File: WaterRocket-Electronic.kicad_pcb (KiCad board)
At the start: 2 copper layers, 60 x 60 mm, 9 parts, among them J1 Screw_Terminal_01x02, SW1 SW_SPDT, U1 MPU_6050

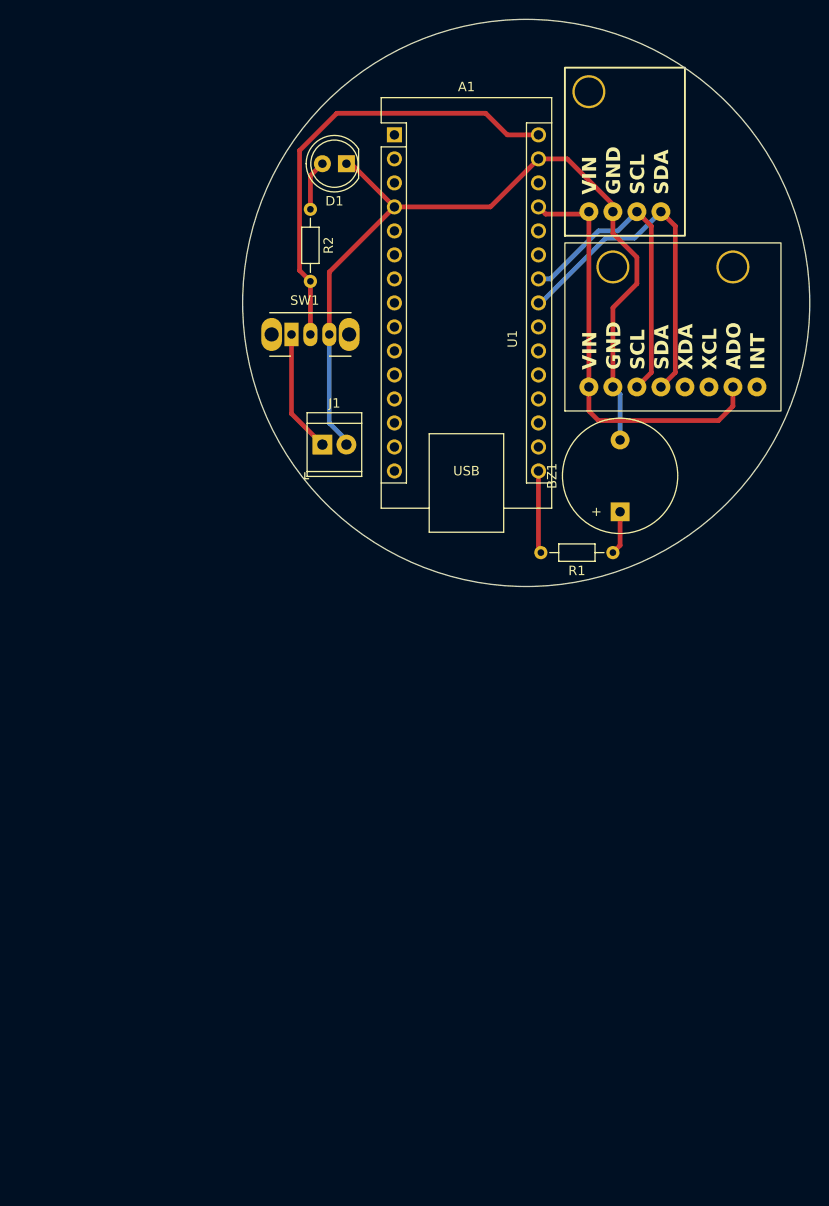
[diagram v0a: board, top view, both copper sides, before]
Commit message: Added servomotor, exported
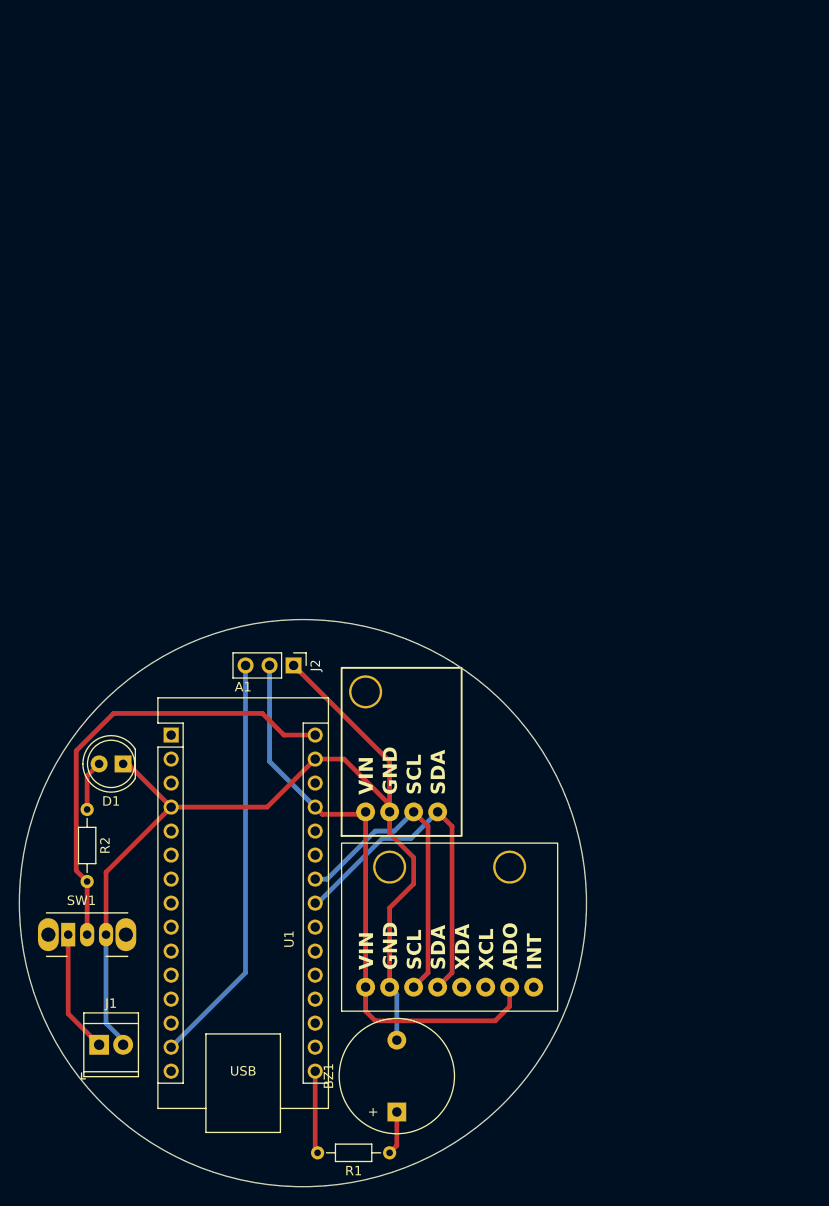
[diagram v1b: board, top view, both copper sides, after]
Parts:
- added J2: Conn_01x03, Connector_PinHeader_2.54mm:PinHeader_1x03_P2.54mm_Vertical, F.Cu at (102.9, 114.8)
- moved J1 67.8 mm to (82.3, 154.9)
- moved R2 67.8 mm to (81.0, 130.0)
- moved SW1 67.8 mm to (79.0, 143.3)
- moved U1 67.8 mm to (110.5, 148.8)
- moved A1 67.8 mm to (89.9, 122.2)
- moved D1 67.8 mm to (84.8, 125.2)
- moved R1 67.8 mm to (113.0, 166.4)
- moved S1 67.8 mm to (110.5, 130.3)
- moved BZ1 67.8 mm to (113.8, 162.1)
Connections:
- A1 pad 14: unconnected-(A1-D11-Pad14) -> /servo_pwm
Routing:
- net /servo_pwm: track 0.00 -> 43.6 mm
- net GND: track 90.3 -> 110.0 mm
- net +5V: track 45.2 -> 62.1 mm

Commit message: dont remember what was updated but committing anyway
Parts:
- added A1: Arduino_Nano_v2.x, Module:Arduino_Nano, F.Cu at (130.6, 204.2)
- added A1: Arduino_Nano_v2.x, Module:Arduino_Nano, F.Cu at (130.6, 37.8)
- added A1: Arduino_Nano_v2.x, Module:Arduino_Nano, F.Cu at (45.5, 38.4)
- added A1: Arduino_Nano_v2.x, Module:Arduino_Nano, F.Cu at (130.7, 118.0)
- added A1: Arduino_Nano_v2.x, Module:Arduino_Nano, F.Cu at (45.5, 204.7)
- added BZ1: Buzzer, Buzzer_Beeper:Buzzer_12x9.5RM7.6, F.Cu at (69.3, 78.2)
- added BZ1: Buzzer, Buzzer_Beeper:Buzzer_12x9.5RM7.6, F.Cu at (154.4, 244.1)
- added BZ1: Buzzer, Buzzer_Beeper:Buzzer_12x9.5RM7.6, F.Cu at (154.4, 77.7)
- added BZ1: Buzzer, Buzzer_Beeper:Buzzer_12x9.5RM7.6, F.Cu at (69.3, 244.6)
- added BZ1: Buzzer, Buzzer_Beeper:Buzzer_12x9.5RM7.6, F.Cu at (154.6, 157.9)
- added D1: LED, LED_THT:LED_D5.0mm, F.Cu at (125.5, 40.9)
- added D1: LED, LED_THT:LED_D5.0mm, F.Cu at (40.4, 207.8)
- added D1: LED, LED_THT:LED_D5.0mm, F.Cu at (125.6, 121.1)
- added D1: LED, LED_THT:LED_D5.0mm, F.Cu at (40.4, 41.4)
- added D1: LED, LED_THT:LED_D5.0mm, F.Cu at (125.5, 207.3)
- added J1: Screw_Terminal_01x02, TerminalBlock_TE-Connectivity:TerminalBlock_TE_282834-2_1x02_P2.54mm_Horizontal, F.Cu at (122.9, 237.0)
- added J1: Screw_Terminal_01x02, TerminalBlock_TE-Connectivity:TerminalBlock_TE_282834-2_1x02_P2.54mm_Horizontal, F.Cu at (37.8, 71.1)
- added J1: Screw_Terminal_01x02, TerminalBlock_TE-Connectivity:TerminalBlock_TE_282834-2_1x02_P2.54mm_Horizontal, F.Cu at (37.8, 237.5)
- added J1: Screw_Terminal_01x02, TerminalBlock_TE-Connectivity:TerminalBlock_TE_282834-2_1x02_P2.54mm_Horizontal, F.Cu at (122.9, 70.6)
- added J1: Screw_Terminal_01x02, TerminalBlock_TE-Connectivity:TerminalBlock_TE_282834-2_1x02_P2.54mm_Horizontal, F.Cu at (123.1, 150.8)
- added J2: Conn_01x03, Connector_PinHeader_2.54mm:PinHeader_1x03_P2.54mm_Vertical, F.Cu at (143.5, 196.8)
- added J2: Conn_01x03, Connector_PinHeader_2.54mm:PinHeader_1x03_P2.54mm_Vertical, F.Cu at (143.5, 30.5)
- added J2: Conn_01x03, Connector_PinHeader_2.54mm:PinHeader_1x03_P2.54mm_Vertical, F.Cu at (58.4, 197.4)
- added J2: Conn_01x03, Connector_PinHeader_2.54mm:PinHeader_1x03_P2.54mm_Vertical, F.Cu at (143.7, 110.7)
- added J2: Conn_01x03, Connector_PinHeader_2.54mm:PinHeader_1x03_P2.54mm_Vertical, F.Cu at (58.4, 31.0)
- added R1: 330, Resistor_THT:R_Axial_DIN0204_L3.6mm_D1.6mm_P7.62mm_Horizontal, F.Cu at (68.6, 248.9)
- added R1: 330, Resistor_THT:R_Axial_DIN0204_L3.6mm_D1.6mm_P7.62mm_Horizontal, F.Cu at (153.7, 248.4)
- added R1: 330, Resistor_THT:R_Axial_DIN0204_L3.6mm_D1.6mm_P7.62mm_Horizontal, F.Cu at (153.7, 82.0)
- added R1: 330, Resistor_THT:R_Axial_DIN0204_L3.6mm_D1.6mm_P7.62mm_Horizontal, F.Cu at (153.8, 162.2)
- added R1: 330, Resistor_THT:R_Axial_DIN0204_L3.6mm_D1.6mm_P7.62mm_Horizontal, F.Cu at (68.6, 82.5)
- added R2: 700, Resistor_THT:R_Axial_DIN0204_L3.6mm_D1.6mm_P7.62mm_Horizontal, F.Cu at (36.6, 46.2)
- added R2: 700, Resistor_THT:R_Axial_DIN0204_L3.6mm_D1.6mm_P7.62mm_Horizontal, F.Cu at (121.8, 125.9)
- added R2: 700, Resistor_THT:R_Axial_DIN0204_L3.6mm_D1.6mm_P7.62mm_Horizontal, F.Cu at (121.7, 212.1)
- added R2: 700, Resistor_THT:R_Axial_DIN0204_L3.6mm_D1.6mm_P7.62mm_Horizontal, F.Cu at (121.7, 45.7)
- added R2: 700, Resistor_THT:R_Axial_DIN0204_L3.6mm_D1.6mm_P7.62mm_Horizontal, F.Cu at (36.6, 212.6)
- added S1: BME280_I2C, Library:BME280_I2C, F.Cu at (152.1, 44.5)
- added S1: BME280_I2C, Library:BME280_I2C, F.Cu at (67.0, 211.4)
- added S1: BME280_I2C, Library:BME280_I2C, F.Cu at (152.3, 124.7)
- added S1: BME280_I2C, Library:BME280_I2C, F.Cu at (152.1, 210.9)
- added S1: BME280_I2C, Library:BME280_I2C, F.Cu at (67.0, 45.0)
- added SW1: SW_SPDT, Button_Switch_THT:SW_CuK_OS102011MA1QN1_SPDT_Angled, F.Cu at (119.8, 139.1)
- added SW1: SW_SPDT, Button_Switch_THT:SW_CuK_OS102011MA1QN1_SPDT_Angled, F.Cu at (34.6, 59.5)
- added SW1: SW_SPDT, Button_Switch_THT:SW_CuK_OS102011MA1QN1_SPDT_Angled, F.Cu at (34.6, 225.8)
- added SW1: SW_SPDT, Button_Switch_THT:SW_CuK_OS102011MA1QN1_SPDT_Angled, F.Cu at (119.7, 59.0)
- added SW1: SW_SPDT, Button_Switch_THT:SW_CuK_OS102011MA1QN1_SPDT_Angled, F.Cu at (119.7, 225.3)
- added U1: MPU_6050, Library:MPU_6050, F.Cu at (83.8, 231.1)
- added U1: MPU_6050, Library:MPU_6050, F.Cu at (168.9, 64.3)
- added U1: MPU_6050, Library:MPU_6050, F.Cu at (169.1, 144.4)
- added U1: MPU_6050, Library:MPU_6050, F.Cu at (168.9, 230.6)
- added U1: MPU_6050, Library:MPU_6050, F.Cu at (83.8, 64.8)
- moved J1 44.4 mm to (38.0, 151.3)
- moved D1 44.4 mm to (40.6, 121.6)
- moved J2 44.4 mm to (58.6, 111.2)
- moved A1 44.4 mm to (45.6, 118.5)
- moved BZ1 44.4 mm to (69.5, 158.4)
- moved R1 44.4 mm to (68.8, 162.7)
- moved R2 44.4 mm to (36.7, 126.4)
- moved SW1 44.4 mm to (34.7, 139.7)
- moved S1 43.6 mm to (67.2, 125.2)
- moved U1 26.8 mm to (84.0, 145.0)
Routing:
- net GND: track 110.0 -> 643.9 mm
- net +5V: track 62.1 -> 389.2 mm
- net /SDA: track 36.8 -> 288.5 mm
- net VCC: track 47.8 -> 292.4 mm
- net /SCL: track 33.2 -> 253.2 mm
- net /servo_pwm: track 43.6 -> 261.9 mm
- net Net-(J1-Pin_1): track 15.1 -> 90.4 mm
- net Net-(A1-D13): track 8.74 -> 52.4 mm
- net Net-(D1-A): track 5.35 -> 32.1 mm
- net Net-(BZ1--): track 4.63 -> 27.8 mm
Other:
- board size 60 x 60 mm -> 145.3 x 226.9 mm
- board text added: "WaterRocket Avionic MkI"
